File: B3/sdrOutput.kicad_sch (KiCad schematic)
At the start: 7 parts, among them U301 74HC04, U302 74HC125, U305 74HC74, U309 74HC00, U313 74HC299, U314 74HC32, U315 74HC193

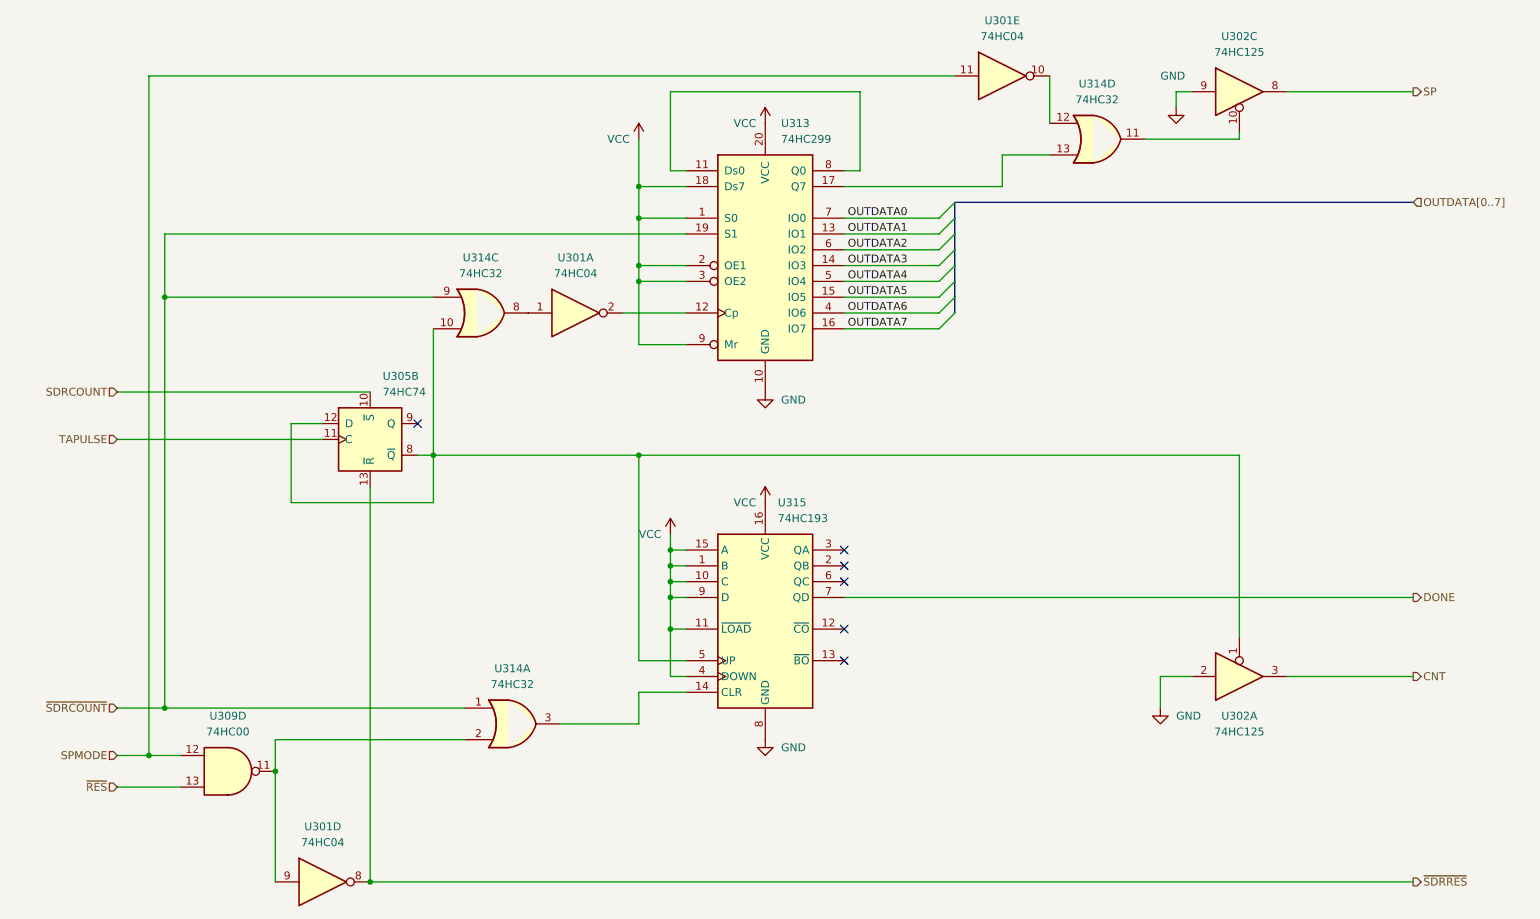
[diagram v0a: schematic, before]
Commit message: B3 added. First revision
Still not verified.
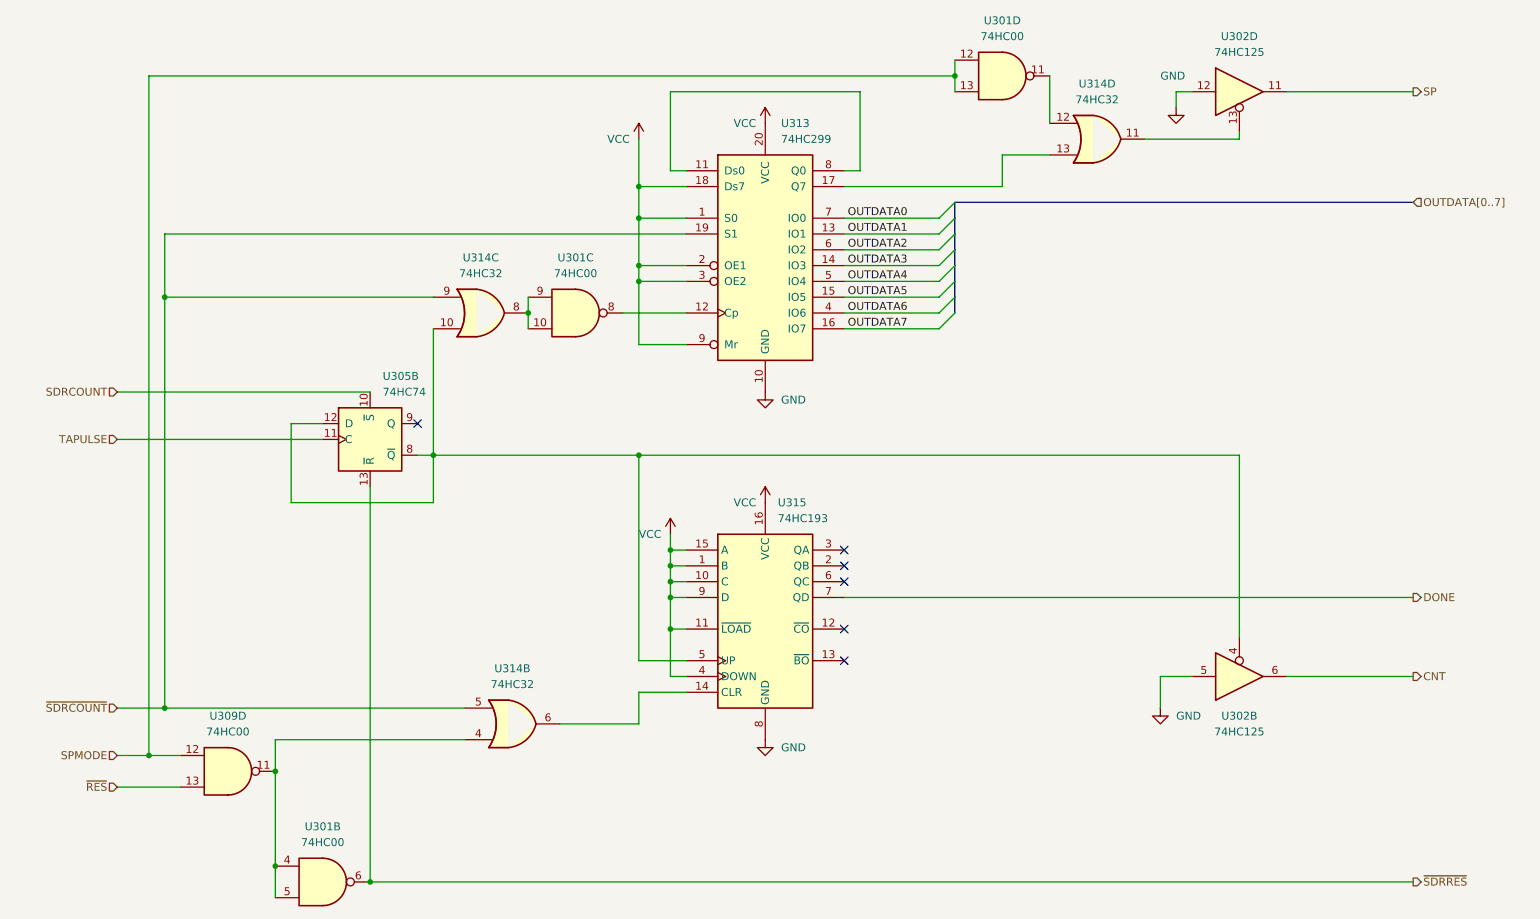
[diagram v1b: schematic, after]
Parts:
- removed U301: 74HC04, Package_SO:SO-14_3.9x8.65mm_P1.27mm, symbol 74xx:74HC04
- removed U302: 74HC125, Package_SO:SO-14_3.9x8.65mm_P1.27mm, symbol 74xx:74LS125
- added U301: 74HC00, Package_SO:SO-14_3.9x8.65mm_P1.27mm, symbol 74xx:74HC00
- added U302: 74HC125, Package_SO:SO-14_3.9x8.65mm_P1.27mm, symbol 74xx:74LS125
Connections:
- net CNT: now also U302.6
- net GND: now also U302.12, U302.5
- net SP: now also U302.11
- net SPMODE: now also U301.12, U301.13
- net ~{SDRCOUNT}: now also U314.5; no longer U314.1
- net ~{SDRRES}: now also U301.6
- net at U315.14 (CLR): now also U314.6; no longer U314.3
- net at U305.12 (D), U305.8 (~{Q}), U314.10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: now also U302.4
- net at U309.11: now also U314.4, U301.4, U301.5; no longer U314.2
- net at U314.8: now also U301.10, U301.9
- net at U314.12: now also U301.11
- net at U313.12 (Cp): now also U301.8
- net at U314.11: now also U302.13

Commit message: .
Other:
- company: (none) -> Daniel Molina
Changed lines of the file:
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@@
   (title_block
     (title "74HCT6526 Board 3")
-    (date "2022-09-11")
-    (rev "0.1")
+    (date "2022-10-08")
+    (rev "0.1.2")
+    (company "Daniel Molina")
+    (comment 1 "https://github.com/dmolinagarcia/74HCT6526")
   )
   (junction (at 175.26 22.86) (diameter 0) (color 0 0 0 0)

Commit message: Release v0.1.2. Added SDR!
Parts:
- removed unit 2 of U314
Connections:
- net ~{SDRCOUNT}: now also U315.14 (CLR)
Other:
- moved on the sheet: U302B, U309D, U314D

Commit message: B0 ready for v0.2.0 release.
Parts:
- added U340: 74HC74, symbol 74xx:74HC74
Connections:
- net VCC: now also U340.1 (~{R}), U340.4 (~{S})
- net ~{SDRCOUNT}: now also U340.2 (D); no longer U313.19 (S1)
- net at U305.12 (D), U305.8 (~{Q}), U314.10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: no longer U302.4
- net at U301.10, U301.9, U314.8: now also U302.4
- new net: U313.19 (S1), U340.5 (Q)
- new net ~{PHI2}: U340.3 (C)
- no-connect marks 6 -> 7
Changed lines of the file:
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@@
   (title_block
     (title "74HCT6526 Board 3")
-    (date "2022-10-08")
-    (rev "0.1.2")
+    (date "2023-01-22")
+    (rev "0.2.0")
     (company "Daniel Molina")
     (comment 1 "https://github.com/dmolinagarcia/74HCT6526")
@@
   (junction (at 81.28 152.4) (diameter 0) (color 0 0 0 0)
   )
-  (junction (at 124.46 83.82) (diameter 0) (color 0 0 0 0)
+  (junction (at 106.68 63.5) (diameter 0) (color 0 0 0 0)
   )
   (junction (at 129.54 106.68) (diameter 0) (color 0 0 0 0)
@@
   (junction (at 129.54 101.6) (diameter 0) (color 0 0 0 0)
   )
+  (no_connect (at 85.09 41.91))
   (no_connect (at 88.9 78.74))
   (no_connect (at 157.48 101.6))
@@
     (stroke (width 0) (type default) (color 0 0 0 0))
   )
+  (wire (pts (xy 85.09 36.83) (xy 106.68 36.83))
+    (stroke (width 0) (type default) (color 0 0 0 0))
+  )
   (wire (pts (xy 157.48 58.42) (xy 172.72 58.42))
     (stroke (width 0) (type default) (color 0 0 0 0))
@@
     (stroke (width 0) (type default) (color 0 0 0 0))
   )
+  (wire (pts (xy 40.64 39.37) (xy 69.85 39.37))
+    (stroke (width 0) (type default) (color 0 0 0 0))
+  )
   (wire (pts (xy 132.08 53.34) (xy 124.46 53.34))
     (stroke (width 0) (type default) (color 0 0 0 0))
@@
     (stroke (width 0) (type default) (color 0 0 0 0))
   )
-  (wire (pts (xy 124.46 83.82) (xy 124.46 116.84))
+  (wire (pts (xy 91.44 83.82) (xy 91.44 116.84))
     (stroke (width 0) (type default) (color 0 0 0 0))
   )
@@
     (stroke (width 0) (type default) (color 0 0 0 0))
   )
-  (wire (pts (xy 124.46 116.84) (xy 132.08 116.84))
+  (wire (pts (xy 91.44 116.84) (xy 132.08 116.84))
     (stroke (width 0) (type default) (color 0 0 0 0))
   )
@@
     (stroke (width 0) (type default) (color 0 0 0 0))
   )
+  (wire (pts (xy 106.68 36.83) (xy 106.68 48.26))
+    (stroke (width 0) (type default) (color 0 0 0 0))
+  )
   (wire (pts (xy 106.68 58.42) (xy 106.68 60.96))
     (stroke (width 0) (type default) (color 0 0 0 0))
@@
     (stroke (width 0) (type default) (color 0 0 0 0))
   )
-  (wire (pts (xy 124.46 83.82) (xy 220.98 83.82))
-    (stroke (width 0) (type default) (color 0 0 0 0))
-  )
   (wire (pts (xy 157.48 40.64) (xy 190.5 40.64))
     (stroke (width 0) (type default) (color 0 0 0 0))
   )
+  (wire (pts (xy 48.26 36.83) (xy 48.26 58.42))
+    (stroke (width 0) (type default) (color 0 0 0 0))
+  )
   (wire (pts (xy 129.54 111.76) (xy 132.08 111.76))
     (stroke (width 0) (type default) (color 0 0 0 0))
@@
     (stroke (width 0) (type default) (color 0 0 0 0))
   )
+  (wire (pts (xy 106.68 48.26) (xy 132.08 48.26))
+    (stroke (width 0) (type default) (color 0 0 0 0))
+  )
   (wire (pts (xy 132.08 66.04) (xy 124.46 66.04))
     (stroke (width 0) (type default) (color 0 0 0 0))
@@
     (stroke (width 0) (type default) (color 0 0 0 0))
   )
+  (wire (pts (xy 48.26 36.83) (xy 69.85 36.83))
+    (stroke (width 0) (type default) (color 0 0 0 0))
+  )
   (wire (pts (xy 88.9 83.82) (xy 91.44 83.82))
     (stroke (width 0) (type default) (color 0 0 0 0))
@@
     (stroke (width 0) (type default) (color 0 0 0 0))
   )
-  (wire (pts (xy 91.44 83.82) (xy 124.46 83.82))
-    (stroke (width 0) (type default) (color 0 0 0 0))
-  )
   (wire (pts (xy 66.04 152.4) (xy 66.04 154.94))
     (stroke (width 0) (type default) (color 0 0 0 0))
@@
     (stroke (width 0) (type default) (color 0 0 0 0))
   )
-  (wire (pts (xy 132.08 48.26) (xy 48.26 48.26))
-    (stroke (width 0) (type default) (color 0 0 0 0))
-  )
   (wire (pts (xy 124.46 40.64) (xy 132.08 40.64))
     (stroke (width 0) (type default) (color 0 0 0 0))
@@
     (stroke (width 0) (type default) (color 0 0 0 0))
   )
+  (wire (pts (xy 106.68 83.82) (xy 220.98 83.82))
+    (stroke (width 0) (type default) (color 0 0 0 0))
+  )
+  (wire (pts (xy 106.68 63.5) (xy 106.68 83.82))
+    (stroke (width 0) (type default) (color 0 0 0 0))
+  )
   (wire (pts (xy 157.48 45.72) (xy 172.72 45.72))
     (stroke (width 0) (type default) (color 0 0 0 0))
@@
   )
   (wire (pts (xy 129.54 38.1) (xy 129.54 25.4))
-    (stroke (width 0) (type default) (color 0 0 0 0))
-  )
-  (wire (pts (xy 48.26 48.26) (xy 48.26 58.42))
     (stroke (width 0) (type default) (color 0 0 0 0))
   )
@@
     (effects (font (size 1.27 1.27)) (justify right bottom))
   )
+  (hierarchical_label "~{PHI2}" (shape input) (at 40.64 39.37 180)
+    (effects (font (size 1.27 1.27)) (justify right))
+  )
   (hierarchical_label "~{RES}" (shape input) (at 40.64 154.94 180)
     (effects (font (size 1.27 1.27)) (justify right))
@@
     (pin "8")
     (pin "9")
+  )
+  (symbol (lib_id "74xx:74HC74") (at 77.47 39.37 0) (unit 1)
+    (in_bom yes) (on_board yes) (fields_autoplaced)
+    (property "Reference" "U340" (id 0) (at 79.4894 30.48 0)
+      (effects (font (size 1.27 1.27)) (justify left))
+    )
+    (property "Value" "74HC74" (id 1) (at 79.4894 33.02 0)
+      (effects (font (size 1.27 1.27)) (justify left))
+    )
+    (property "Footprint" "" (id 2) (at 77.47 39.37 0)
+      (effects (font (size 1.27 1.27)) hide)
+    )
+    (property "Datasheet" "74xx/74hc_hct74.pdf" (id 3) (at 77.47 39.37 0)
+      (effects (font (size 1.27 1.27)) hide)
+    )
+    (pin "1")
+    (pin "2")
+    (pin "3")
+    (pin "4")
+    (pin "5")
+    (pin "6")
+    (pin "10")
+    (pin "11")
+    (pin "12")
+    (pin "13")
+    (pin "8")
+    (pin "9")
+    (pin "14")
+    (pin "7")
   )
   (symbol (lib_id "74xx:74HC00") (at 114.3 60.96 0) (unit 3)
@@
     (pin "14")
     (pin "7")
+  )
+  (symbol (lib_id "power:VCC") (at 77.47 46.99 180) (unit 1)
+    (in_bom yes) (on_board yes)
+    (property "Reference" "#PWR0361" (id 0) (at 77.47 43.18 0)
+      (effects (font (size 1.27 1.27)) hide)
+    )
+    (property "Value" "VCC" (id 1) (at 82.55 46.99 0)
+      (effects (font (size 1.27 1.27)) (justify left))
+    )
+    (property "Footprint" "" (id 2) (at 77.47 46.99 0)
+      (effects (font (size 1.27 1.27)) hide)
+    )
+    (property "Datasheet" "" (id 3) (at 77.47 46.99 0)
+      (effects (font (size 1.27 1.27)) hide)
+    )
+    (pin "1")
   )
   (symbol (lib_id "74xx:74HC74") (at 81.28 81.28 0) (unit 2)
@@
       (effects (font (size 1.27 1.27)) hide)
     )
+    (pin "1")
+  )
+  (symbol (lib_id "power:VCC") (at 77.47 31.75 0) (unit 1)
+    (in_bom yes) (on_board yes)
+    (property "Reference" "#PWR0360" (id 0) (at 77.47 35.56 0)
+      (effects (font (size 1.27 1.27)) hide)
+    )
+    (property "Value" "VCC" (id 1) (at 72.39 31.75 0)
+      (effects (font (size 1.27 1.27)) (justify left))
+    )
+    (property "Footprint" "" (id 2) (at 77.47 31.75 0)
+      (effects (font (size 1.27 1.27)) hide)
+    )
+    (property "Datasheet" "" (id 3) (at 77.47 31.75 0)
+      (effects (font (size 1.27 1.27)) hide)
+    )

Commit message: B3 ready for v0.2.0 release
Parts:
- U340: footprint (none) -> Package_SO:SO-14_3.9x8.65mm_P1.27mm
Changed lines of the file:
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@@
       (effects (font (size 1.27 1.27)) (justify left))
     )
-    (property "Footprint" "" (id 2) (at 77.47 39.37 0)
+    (property "Footprint" "Package_SO:SO-14_3.9x8.65mm_P1.27mm" (id 2) (at 77.47 39.37 0)
       (effects (font (size 1.27 1.27)) hide)
     )

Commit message: .
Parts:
- U302: value 74HC125 -> 74HCT125
- U305: value 74HC74 -> 74HCT74
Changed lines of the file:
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@@
       (effects (font (size 1.27 1.27)) (justify left))
     )
-    (property "Value" "74HC74" (id 1) (at 83.2994 73.66 0)
+    (property "Value" "74HCT74" (id 1) (at 83.2994 73.66 0)
       (effects (font (size 1.27 1.27)) (justify left))
     )
@@
     (in_bom yes) (on_board yes) (fields_autoplaced)
     (property "Reference" "U302" (id 0) (at 220.98 99.695 0))
-    (property "Value" "74HC125" (id 1) (at 220.98 102.235 0))
+    (property "Value" "74HCT125" (id 1) (at 220.98 102.235 0))
     (property "Footprint" "Package_SO:SO-14_3.9x8.65mm_P1.27mm" (id 2) (at 220.98 93.345 0)
       (effects (font (size 1.27 1.27)) hide)
@@
     (in_bom yes) (on_board yes) (fields_autoplaced)
     (property "Reference" "U302" (id 0) (at 220.98 16.51 0))
-    (property "Value" "74HC125" (id 1) (at 220.98 19.05 0))
+    (property "Value" "74HCT125" (id 1) (at 220.98 19.05 0))
     (property "Footprint" "Package_SO:SO-14_3.9x8.65mm_P1.27mm" (id 2) (at 220.98 25.4 0)
       (effects (font (size 1.27 1.27)) hide)
